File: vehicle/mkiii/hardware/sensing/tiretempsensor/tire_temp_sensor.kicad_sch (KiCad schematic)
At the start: 28 parts, among them J2 J_PCIe_x1, J3 J_Programming_Pin_Header, U1 STM32G441KBT6, U2 MCP2561-E_SN, Y1 X_16MHz_18pF

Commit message: submitting final pcb board, ready for review (changed name too)
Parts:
- added C8, C9: C_10uF_10V, OEM:C_0603_1608Metric, symbol OEM:C_10uF_10V_0603
- added F1, F3: F_500mA_8V, OEM:Fuse_1206_3216Metric, symbol OEM:F_500mA_8V_1206
- added TP4, TP5: TP_SMD, OEM:TP_Hook_SMD, symbol OEM:TP_Hook_SMD
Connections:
- net +3.3V: now also C8.1, F3.1; no longer J2.A2 (3.3V)
- net +5V: now also C9.1, F1.1; no longer J2.B5 (5V)
- net CAN_+: now also TP5.1
- net CAN_-: now also TP4.1
- net GND: now also C8.2, C9.2; no longer J2.B1 (SCL/SCK), J2.B10 (io_9), J2.B11 (io_11), J2.B12 (io_13), J2.B13 (io_15), J2.B15 (io_19), J2.B16 (io_21), J2.B17 (SHDN_OUT/io_23), J2.B18 (SHDN_OUT/io_25), J2.B2 (SDA/MISO/RX), J2.B3 (MOSI/TX), J2.B6 (io_1), J2.B7 (io_3), J2.B8 (io_5), J2.B9 (io_7)
- new net: F3.2, J2.A2 (3.3V)
- new net: F1.2, J2.B5 (5V)
- no-connect marks 29 -> 45
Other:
- moved on the sheet: TP1, TP3

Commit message: Schematics and PCB Layout are Preliminarily Approved - DRC and ERC results are good.
Changes:
- Updated Title Block
- Added Sensor Info
- Removed extra GND test point (TP6)

Good work Luke!
I2C Calculation looks good!
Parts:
- removed TP6: TP_SMD, OEM:TP_Hook_SMD, symbol OEM:TP_Hook_SMD
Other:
- note added: "Sensor Information: MPN: MLX90640 Manufacturer: Melexis Datasheet: https://media.melexis.com/-/media/files/documents/datasheets/mlx90640-datasheet-melexis.pdf Pinout: 1 SDA 2 VDD (5V; provided by motherboard) 3 GND (provided by motherboard) 4 SCL"
- title: (none) -> Tire Temperature Sensor

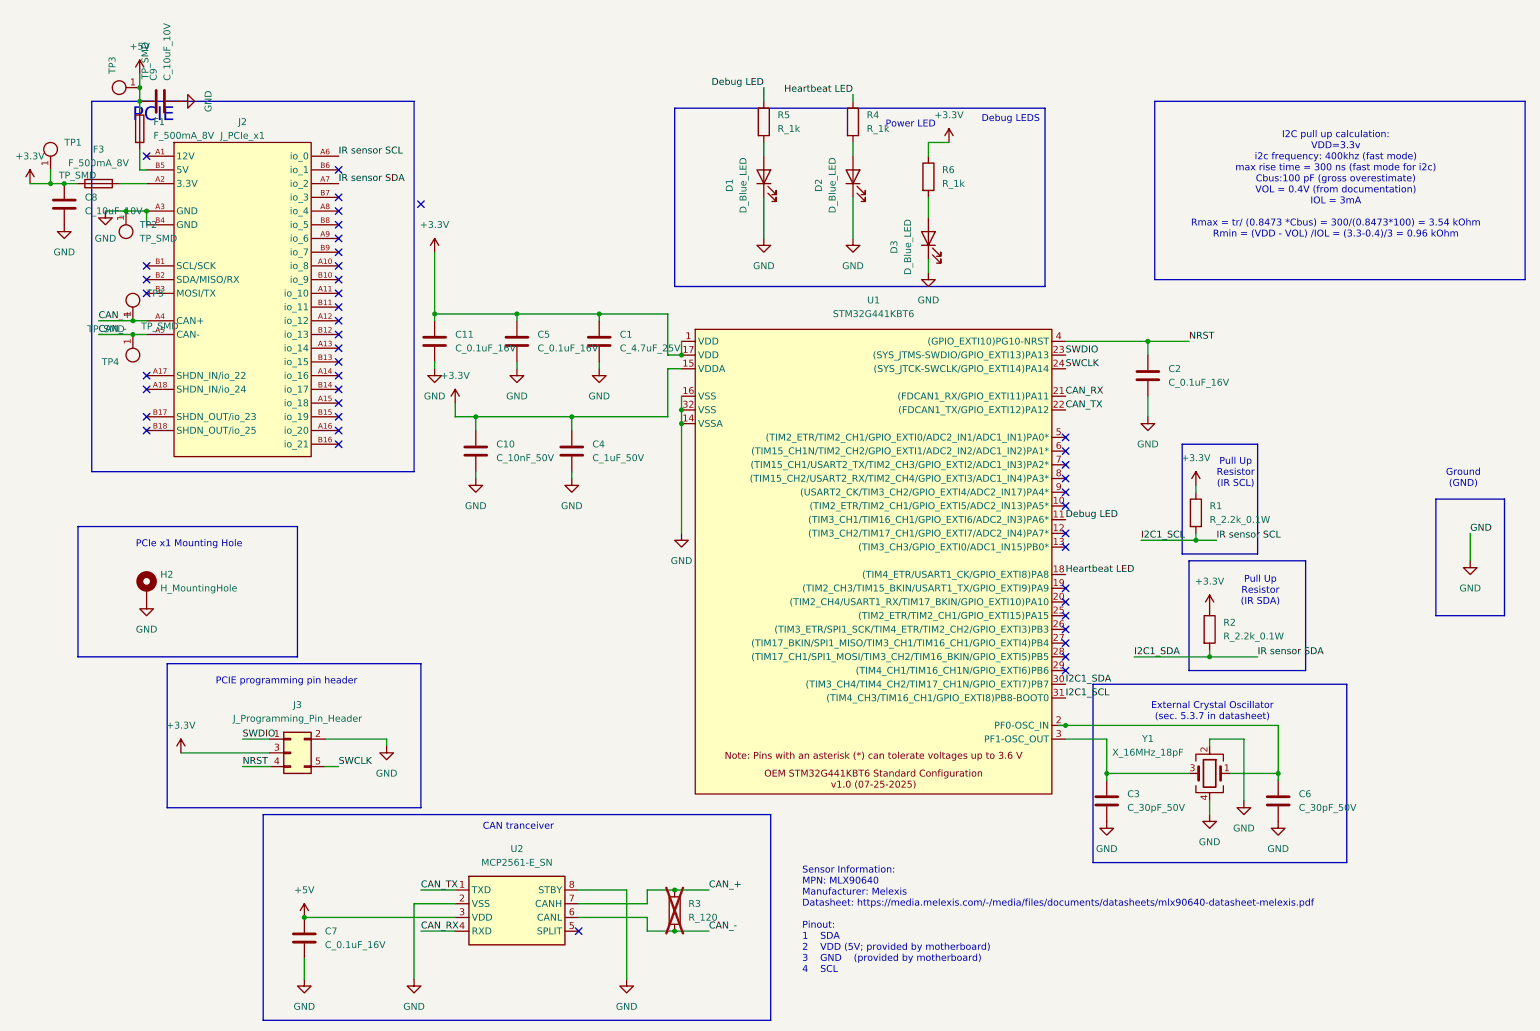
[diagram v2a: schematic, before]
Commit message: added 5V LED, rounded corners, deleted unnecessary silkscreen text created more space between the CAN+ and CAN- testpoints, CAN+ and CAN- test points now face the same direction, cleaned up schematic
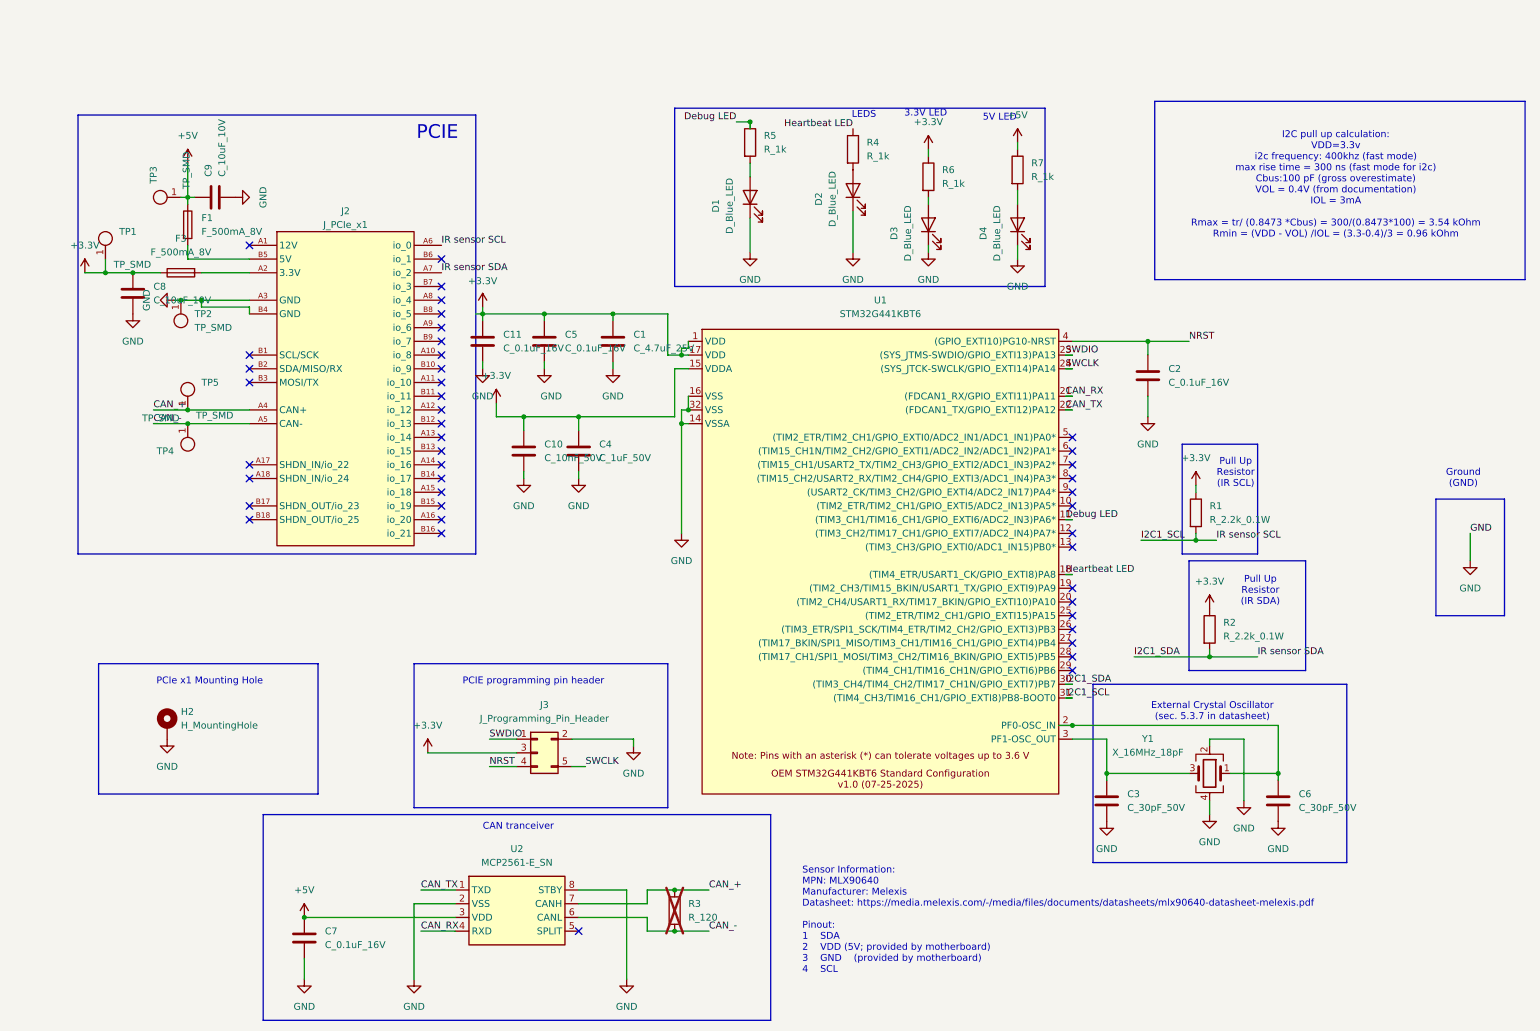
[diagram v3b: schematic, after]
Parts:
- added D4: D_Blue_LED, OEM:D_0805_2012Metric, symbol OEM:D_LED_Blue_0805
- added R7: R_1k, OEM:R_0603_1608Metric, symbol OEM:R_1k_0.1W_0603
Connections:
- net +5V: now also R7.1
- net GND: now also D4.1 (K)
- new net: D4.2 (A), R7.2
- no-connect marks 45 -> 44
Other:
- note added: "3.3V LED"
- note added: "5V LED"
- note added: "LEDS"
- note removed: "Debug LEDS"
- note removed: "Power LED"
- moved on the sheet: C1, C10, C11, C4, C5, C8, C9, D1, D2, D3, F1, F3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
